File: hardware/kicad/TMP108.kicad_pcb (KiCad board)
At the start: 2 copper layers, 75 x 75 mm, 38 parts, among them J1 Screw_Terminal_01x08, J2 Screw_Terminal_01x08, J3 CAN, SW1 PRG, SW2 BUS, SW3 PRG-VALUE, U1 Teensy_3.2, U2 TMR-1211, U3 MCP2551-I-P

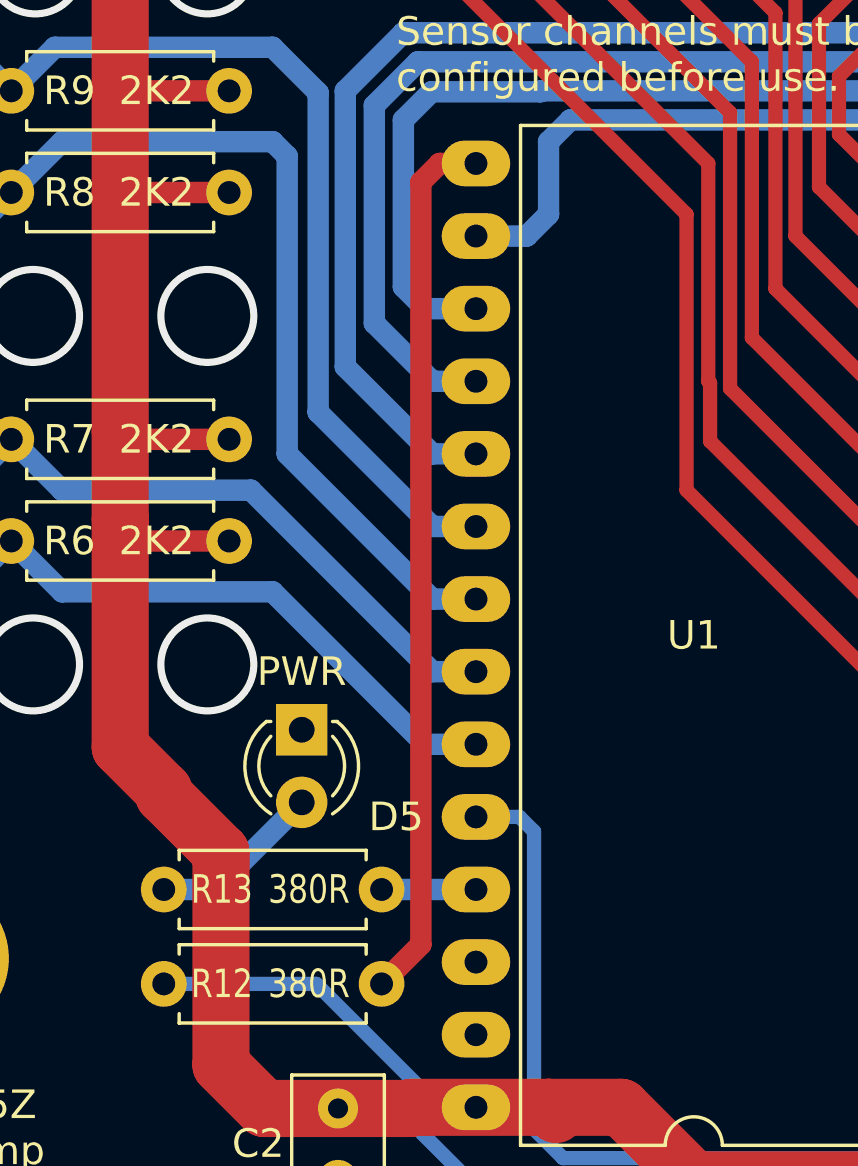
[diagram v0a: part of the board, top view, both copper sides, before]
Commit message: Reassign LED GPIO
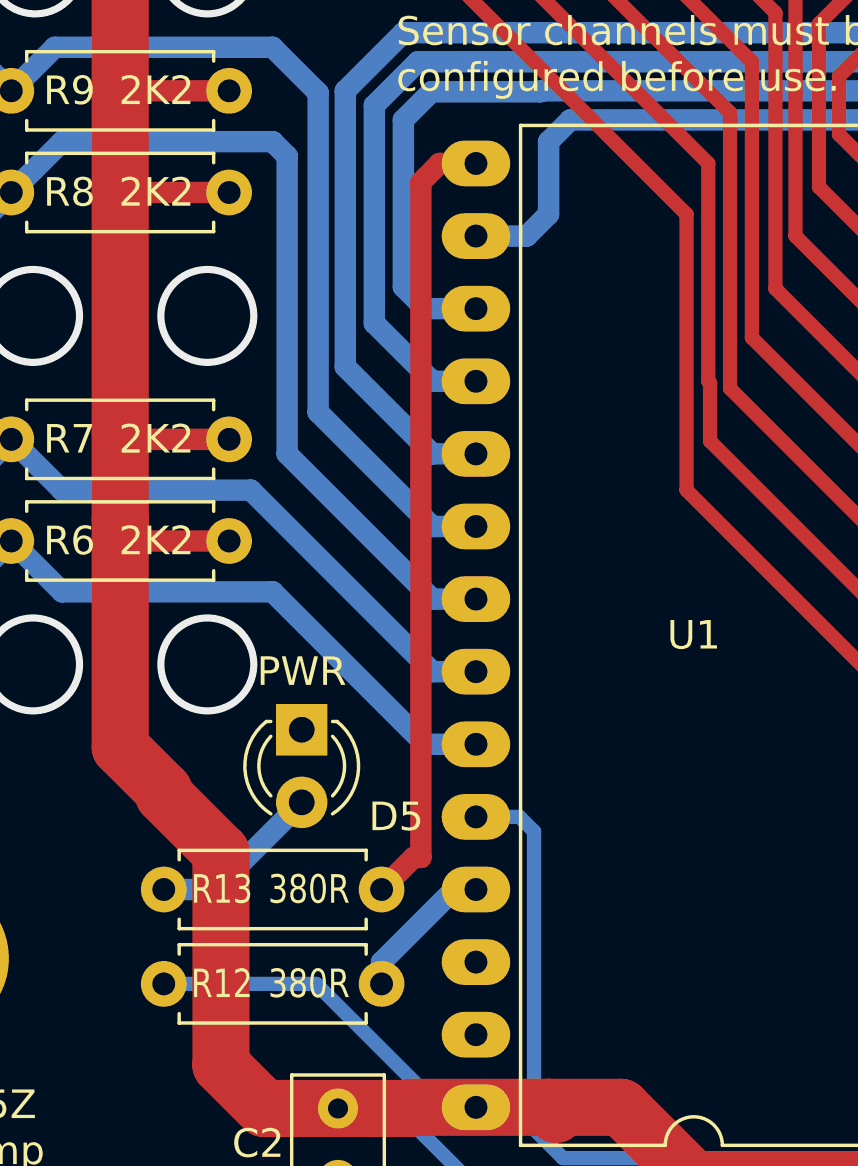
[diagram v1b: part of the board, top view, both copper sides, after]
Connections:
- U1 pad 15: /LED_INTERVAL -> /LED_PWR
- U1 pad 25: /LED_PWR -> /LED_INTERVAL
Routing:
- net /LED_INTERVAL: track 30.8 -> 5.12 mm
- net /LED_PWR: track 3.30 -> 27.7 mm

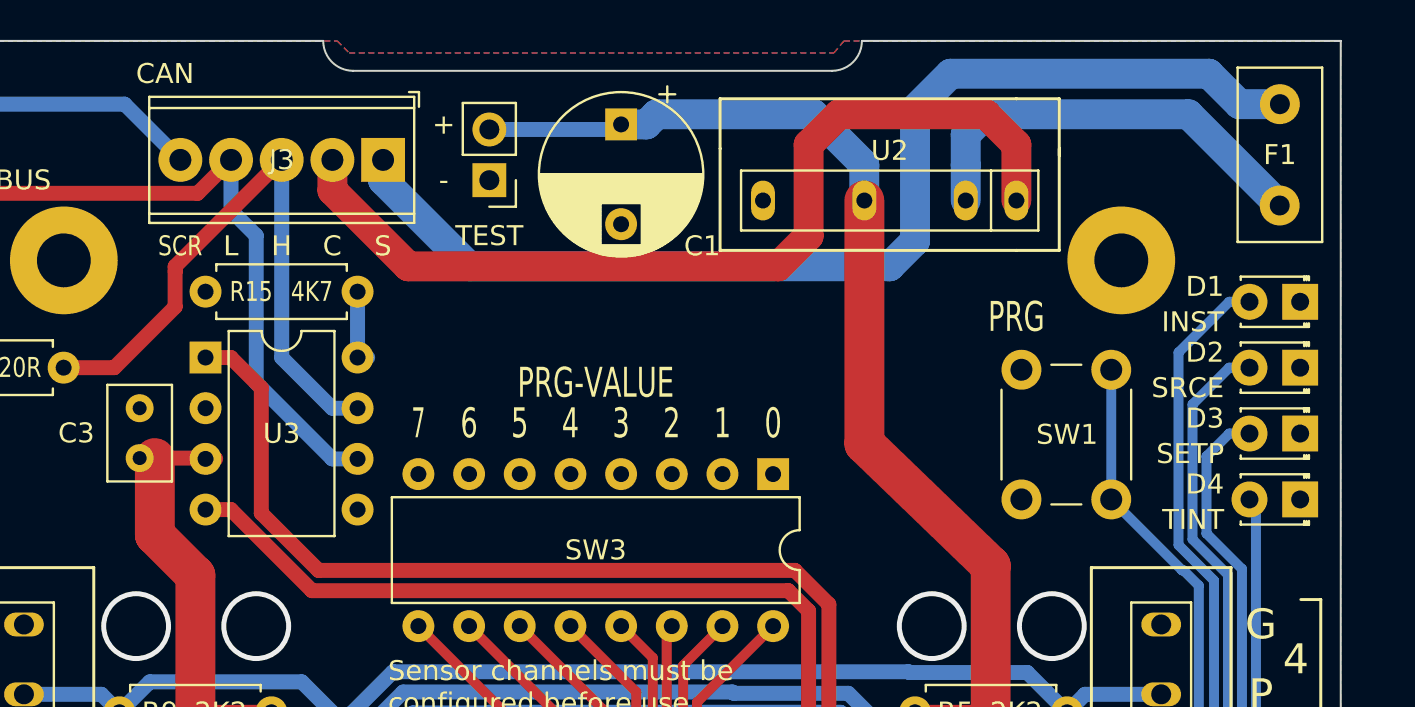
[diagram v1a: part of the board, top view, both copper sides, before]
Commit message: Reroute PCB.
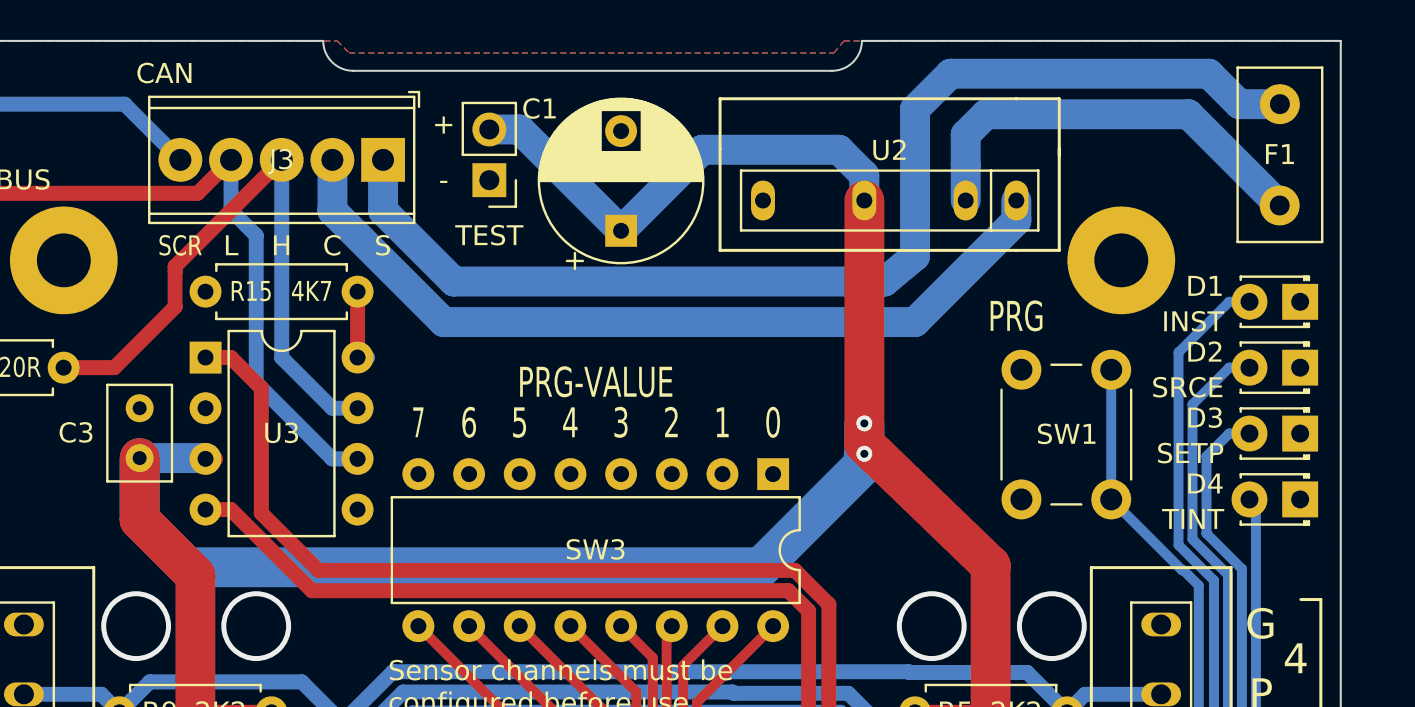
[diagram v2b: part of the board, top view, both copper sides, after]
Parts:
- moved C1 5.33 mm to (174.9, 96.5), turned to 90 degrees
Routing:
- net +5V: track 210.1 -> 257.7 mm, vias 0 -> 2
- net /NET_C: track 46.7 -> 42.3 mm
- net /NET_S: track 56.3 -> 58.2 mm

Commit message: Twaeks,
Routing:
- net /ADDR_2: track 14.6 -> 15.7 mm
- net GND: vias 12 -> 13
- net (no net): vias 0 -> 6

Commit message: Tweaks
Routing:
- net /ADDR_1: track 12.9 -> 16.4 mm
- net GND: vias 13 -> 19
- net (no net): vias 6 -> 0
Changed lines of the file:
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@@
     (thickness 1.6)
     (drawings 144)
-    (tracks 338)
+    (tracks 343)
     (zones 0)
     (modules 38)
@@
     (effects (font (size 1.5 1) (thickness 0.2)))
   )
-  (via (at 178.486 138.43) (size 0.8) (drill 0.4) (layers F.Cu B.Cu) (net 0))
-  (via (at 178.486 135.89) (size 0.8) (drill 0.4) (layers F.Cu B.Cu) (net 0))
-  (via (at 178.486 133.35) (size 0.8) (drill 0.4) (layers F.Cu B.Cu) (net 0))
-  (via (at 178.486 130.81) (size 0.8) (drill 0.4) (layers F.Cu B.Cu) (net 0))
-  (via (at 178.486 128.27) (size 0.8) (drill 0.4) (layers F.Cu B.Cu) (net 0))
-  (via (at 178.486 125.73) (size 0.8) (drill 0.4) (layers F.Cu B.Cu) (net 0))
+  (via (at 178.486 138.43) (size 0.8) (drill 0.4) (layers F.Cu B.Cu) (net 1))
+  (via (at 178.486 135.89) (size 0.8) (drill 0.4) (layers F.Cu B.Cu) (net 1))
+  (via (at 178.486 133.35) (size 0.8) (drill 0.4) (layers F.Cu B.Cu) (net 1))
+  (via (at 178.486 130.81) (size 0.8) (drill 0.4) (layers F.Cu B.Cu) (net 1))
+  (via (at 178.486 128.27) (size 0.8) (drill 0.4) (layers F.Cu B.Cu) (net 1))
+  (via (at 178.486 125.73) (size 0.8) (drill 0.4) (layers F.Cu B.Cu) (net 1))
   (via (at 178.486 123.19) (size 0.8) (drill 0.4) (layers F.Cu B.Cu) (net 1))
   (via (at 156.642 128.524) (size 3.5) (drill 3) (layers F.Cu B.Cu) (net 1))
@@
   (segment (start 177.47 117.348) (end 175.946 118.872) (width 0.5) (layer F.Cu) (net 24))
   (segment (start 177.47 116.332) (end 177.47 117.348) (width 0.5) (layer F.Cu) (net 24))
-  (segment (start 177.47 123.444) (end 179.756 125.73) (width 0.25) (layer F.Cu) (net 25))
-  (segment (start 177.47 119.888) (end 177.47 123.444) (width 0.25) (layer F.Cu) (net 25))
-  (segment (start 180.01 117.348) (end 177.47 119.888) (width 0.25) (layer F.Cu) (net 25))
-  (segment (start 180.01 116.332) (end 180.01 117.348) (width 0.25) (layer F.Cu) (net 25))
-  (segment (start 179.756 125.73) (end 181.28 125.73) (width 0.25) (layer F.Cu) (net 25))
-  (segment (start 182.55 116.332) (end 182.55 117.348) (width 0.25) (layer F.Cu) (net 26))
-  (segment (start 182.55 117.348) (end 178.994 120.904) (width 0.25) (layer F.Cu) (net 26))
-  (segment (start 178.994 120.904) (end 178.994 122.428) (width 0.25) (layer F.Cu) (net 26))
-  (segment (start 178.994 122.428) (end 179.756 123.19) (width 0.25) (layer F.Cu) (net 26))
-  (segment (start 179.756 123.19) (end 181.28 123.19) (width 0.25) (layer F.Cu) (net 26))
+  (segment (start 179.756 125.73) (end 179.629 125.603) (width 0.5) (layer F.Cu) (net 25))
+  (segment (start 181.28 125.73) (end 179.756 125.73) (width 0.5) (layer F.Cu) (net 25))
+  (segment (start 177.47 123.444) (end 179.629 125.603) (width 0.25) (layer F.Cu) (net 25))
+  (segment (start 179.756 125.718002) (end 177.47 123.432002) (width 0.5) (layer F.Cu) (net 25))
+  (segment (start 179.756 125.73) (end 179.756 125.718002) (width 0.5) (layer F.Cu) (net 25))
+  (segment (start 177.47 123.432002) (end 177.47 123.19) (width 0.5) (layer F.Cu) (net 25))
+  (segment (start 177.47 123.19) (end 177.47 123.444) (width 0.25) (layer F.Cu) (net 25))
+  (segment (start 177.47 123.19) (end 177.47 119.888) (width 0.5) (layer F.Cu) (net 25))
+  (segment (start 177.47 119.888) (end 180.01 117.348) (width 0.5) (layer F.Cu) (net 25))
+  (segment (start 180.01 117.348) (end 180.01 116.332) (width 0.5) (layer F.Cu) (net 25))
+  (segment (start 181.28 123.19) (end 179.756 123.19) (width 0.5) (layer F.Cu) (net 26))
+  (segment (start 179.756 123.19) (end 178.994 122.428) (width 0.5) (layer F.Cu) (net 26))
+  (segment (start 178.994 122.428) (end 178.994 120.904) (width 0.5) (layer F.Cu) (net 26))
+  (segment (start 178.994 120.904) (end 182.55 117.348) (width 0.5) (layer F.Cu) (net 26))
+  (segment (start 182.55 117.348) (end 182.55 116.332) (width 0.5) (layer F.Cu) (net 26))
   (segment (start 202.87 112.268) (end 202.87 102.616) (width 0.5) (layer B.Cu) (net 27))
   (segment (start 204.648 114.046) (end 202.87 112.268) (width 0.5) (layer B.Cu) (net 27))
@@
     (connect_pads (clearance 0.508))
     (min_thickness 0.254)
-    (fill (arc_segments 32) (thermal_gap 0.508) (thermal_bridge_width 0.508))
+    (fill yes (arc_segments 32) (thermal_gap 0.508) (thermal_bridge_width 0.508))
     (polygon
       (pts
@@
     (connect_pads (clearance 0.508))
     (min_thickness 0.254)
-    (fill (arc_segments 32) (thermal_gap 0.508) (thermal_bridge_width 0.508))
+    (fill yes (arc_segments 32) (thermal_gap 0.508) (thermal_bridge_width 0.508))
     (polygon
       (pts

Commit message: Isolate temperature sensors
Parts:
- removed D3: SETP, LED_THT:LED_D1.8mm_W3.3mm_H2.4mm
- removed D4: TINT, LED_THT:LED_D1.8mm_W3.3mm_H2.4mm
- removed D5: PWR, LED_THT:LED_D3.0mm_FlatTop
- removed F1: 1A, Fuse:Fuse_Littelfuse_395Series
- removed R10, R11, R12, R13: 380R, Resistor_THT:R_Axial_DIN0207_L6.3mm_D2.5mm_P7.62mm_Horizontal
- removed R14: 120R, Resistor_THT:R_Axial_DIN0207_L6.3mm_D2.5mm_P7.62mm_Horizontal
- removed R15: 4K7, Resistor_THT:R_Axial_DIN0207_L6.3mm_D2.5mm_P7.62mm_Horizontal
- removed R3, R4, R5, R6, R7, R8, R9: 2K2, Resistor_THT:R_Axial_DIN0207_L6.3mm_D2.5mm_P7.62mm_Horizontal
- removed the REF** at (200.0, 151.0)
- removed the REF** at (147.0, 151.0)
- removed the REF** at (147.0, 98.0)
- removed the REF** at (200.0, 98.0)
- removed SW1: PRG, Button_Switch_THT:SW_PUSH_6mm_H4.3mm
- removed SW2: BUS, Package_DIP:DIP-4_W7.62mm_LongPads
- removed SW3: PRG-VALUE, Package_DIP:DIP-16_W7.62mm
- removed TEST: PinHeader_1x02_P2.54mm_Vertical, Connector_PinHeader_2.54mm:PinHeader_1x02_P2.54mm_Vertical
- added C101: 100nF, Capacitor_THT:CP_Radial_D5.0mm_P2.50mm, F.Cu at (108.7, -158.1)
- added C102: 100nF, Capacitor_SMD:C_0805_2012Metric, F.Cu at (92.5, -142.5)
- added C103: 100nF, Capacitor_SMD:C_0805_2012Metric, F.Cu at (121.3, -124.1)
- added C104: 100nF, Capacitor_SMD:C_0805_2012Metric, F.Cu at (146.8, -137.5)
- added C105: 100nF, Capacitor_SMD:C_0805_2012Metric, F.Cu at (146.8, -125.5)
- added C4: 20nF, Capacitor_SMD:C_0805_2012Metric, F.Cu at (90.6, -86.1)
- added D101: LED, LED_THT:LED_D1.8mm_W3.3mm_H2.4mm, F.Cu at (166.2, -146.7)
- added D102: LED, LED_THT:LED_D1.8mm_W3.3mm_H2.4mm, F.Cu at (166.2, -143.4)
- added D103: LED, LED_THT:LED_D1.8mm_W3.3mm_H2.4mm, F.Cu at (166.2, -136.8)
- added D104: LED, LED_THT:LED_D1.8mm_W3.3mm_H2.4mm, F.Cu at (166.2, -130.2)
- added D105: LED, LED_THT:LED_D1.8mm_W3.3mm_H2.4mm, F.Cu at (166.2, -123.6)
- added D110: LED, LED_THT:LED_D1.8mm_W3.3mm_H2.4mm, F.Cu at (166.2, -140.1)
- added D111: LED, LED_THT:LED_D1.8mm_W3.3mm_H2.4mm, F.Cu at (166.2, -133.5)
- added D112: LED, LED_THT:LED_D1.8mm_W3.3mm_H2.4mm, F.Cu at (166.2, -126.9)
- added D113: LED, LED_THT:LED_D1.8mm_W3.3mm_H2.4mm, F.Cu at (166.2, -120.3)
- added F101: 1A, Fuse:Fuse_Littelfuse_395Series, F.Cu at (81.2, -152.2)
- added J101: CAN, Connector_PinHeader_2.54mm:PinHeader_1x05_P2.54mm_Vertical, F.Cu at (75.7, -147.5)
- added J4: Screw_Terminal_01x03, Connector_PinHeader_2.54mm:PinHeader_1x03_P2.54mm_Vertical, F.Cu at (124.1, -80.6)
- added J5: Screw_Terminal_01x03, Connector_PinHeader_2.54mm:PinHeader_1x03_P2.54mm_Vertical, F.Cu at (134.3, -80.6)
- added J6: Screw_Terminal_01x03, Connector_PinHeader_2.54mm:PinHeader_1x03_P2.54mm_Vertical, F.Cu at (144.5, -80.6)
- added Q101: BSS138, Package_TO_SOT_SMD:SOT-23, F.Cu at (100.4, -141.8)
- added Q102: BSS138, Package_TO_SOT_SMD:SOT-23, F.Cu at (100.4, -134.6)
- added R101: 10K 0.125W, Resistor_SMD:R_0805_2012Metric, F.Cu at (103.4, -134.6)
- added R102: 10K 0.125W, Resistor_SMD:R_0805_2012Metric, F.Cu at (103.4, -141.8)
- added R103: 10K 0.125W, Resistor_SMD:R_0805_2012Metric, F.Cu at (96.8, -142.6)
- added R104: 10K 0.125W, Resistor_SMD:R_0805_2012Metric, F.Cu at (96.8, -133.8)
- added R105: 560R, Resistor_SMD:R_0805_2012Metric, F.Cu at (169.2, -146.7)
- added R106: 4K7 0.125W, Resistor_SMD:R_0805_2012Metric, F.Cu at (84.1, -138.4)
- added R107: 120R 0.5W, Resistor_THT:R_Axial_DIN0207_L6.3mm_D2.5mm_P7.62mm_Horizontal, F.Cu at (84.8, -147.5)
- added R108: 4K7 0.125W, Resistor_SMD:R_0805_2012Metric, B.Cu at (162.9, -154.7)
- added R109: 4K7 0.125W, Resistor_SMD:R_0805_2012Metric, B.Cu at (160.4, -154.7)
- added R110: 4K7 0.125W, Resistor_SMD:R_0805_2012Metric, B.Cu at (157.9, -154.7)
- added R111: 4K7 0.125W, Resistor_SMD:R_0805_2012Metric, B.Cu at (155.3, -154.7)
- added R112: 4K7 0.125W, Resistor_SMD:R_0805_2012Metric, B.Cu at (152.8, -154.7)
- added R113: 4K7 0.125W, Resistor_SMD:R_0805_2012Metric, B.Cu at (150.2, -154.7)
- added R114: 4K7 0.125W, Resistor_SMD:R_0805_2012Metric, B.Cu at (147.7, -154.7)
- added R115: 4K7 0.125W, Resistor_SMD:R_0805_2012Metric, B.Cu at (145.2, -154.7)
- added R116: 560R, Resistor_SMD:R_0805_2012Metric, F.Cu at (169.2, -143.4)
- added R117: 560R, Resistor_SMD:R_0805_2012Metric, F.Cu at (169.2, -140.1)
- added R118: 560R, Resistor_SMD:R_0805_2012Metric, F.Cu at (169.2, -136.8)
- added R119: 560R, Resistor_SMD:R_0805_2012Metric, F.Cu at (169.2, -133.5)
- added R120: 560R, Resistor_SMD:R_0805_2012Metric, F.Cu at (169.2, -130.2)
- added R121: 560R, Resistor_SMD:R_0805_2012Metric, F.Cu at (169.2, -127.0)
- added R122: 560R, Resistor_SMD:R_0805_2012Metric, F.Cu at (169.2, -123.6)
- added R123: 560R, Resistor_SMD:R_0805_2012Metric, F.Cu at (169.2, -120.3)
- added REF**: MountingHole_3.2mm_M3_DIN965_Pad_TopBottom, MountingHole:MountingHole_3.2mm_M3_DIN965_Pad_TopBottom, F.Cu at (167.6, -82.4)
- added REF**: MountingHole_3.2mm_M3_DIN965_Pad_TopBottom, MountingHole:MountingHole_3.2mm_M3_DIN965_Pad_TopBottom, F.Cu at (75.6, -153.4)
- added REF**: MountingHole_3.2mm_M3_DIN965_Pad_TopBottom, MountingHole:MountingHole_3.2mm_M3_DIN965_Pad_TopBottom, F.Cu at (167.6, -153.4)
- added REF**: MountingHole_3.2mm_M3_DIN965_Pad_TopBottom, MountingHole:MountingHole_3.2mm_M3_DIN965_Pad_TopBottom, F.Cu at (75.6, -82.4)
- added REF**: TestPoint_THTPad_1.5x1.5mm_Drill0.7mm, TestPoint:TestPoint_THTPad_1.5x1.5mm_Drill0.7mm, F.Cu at (74.8, -133.3)
- added SW101: BUS, Package_DIP:DIP-4_W7.62mm_LongPads, F.Cu at (96.5, -147.9)
- added SW102: ADDR/VALUE, Package_DIP:DIP-16_W7.62mm, F.Cu at (145.2, -150.9)
- added SW103: PRG, Button_Switch_THT:SW_TH_Tactile_Omron_B3F-10xx, F.Cu at (112.8, -156.0)
- added TEST 5V0: TestPoint_THTPad_1.5x1.5mm_Drill0.7mm, TestPoint:TestPoint_THTPad_1.5x1.5mm_Drill0.7mm, F.Cu at (81.2, -133.3)
- added TEST 5V0: TestPoint_THTPad_1.5x1.5mm_Drill0.7mm, TestPoint:TestPoint_THTPad_1.5x1.5mm_Drill0.7mm, F.Cu at (78.0, -133.3)
- added U101: TMR-2-2411, PDJR_DC-DC_Converters:TMR_2411, F.Cu at (85.9, -156.0)
- added U102: MCP2551-I-P, Package_SO:SOIC-8_3.9x4.9mm_P1.27mm, F.Cu at (87.5, -142.5)
- added U103: Teensy_4.0, Package_DIP:DIP-28_W15.24mm_LongPads, F.Cu at (139.3, -123.0)
- added U104: 74HC165, Package_SO:SO-16_3.9x9.9mm_P1.27mm, F.Cu at (151.8, -142.9)
- added U105: 74HCT595, Package_SO:SO-16_3.9x9.9mm_P1.27mm, F.Cu at (151.8, -130.9)
- C1: value 1000uF -> 10uF; footprint Capacitor_THT:CP_Radial_D8.0mm_P5.00mm -> Capacitor_SMD:C_0805_2012Metric
- C2: value 100nF -> 20nF; footprint Capacitor_THT:C_Rect_L4.6mm_W3.0mm_P2.50mm_MKS02_FKP02 -> Capacitor_SMD:C_0805_2012Metric
- C3: value 100n -> 10uF; footprint Capacitor_THT:C_Rect_L4.6mm_W3.0mm_P2.50mm_MKS02_FKP02 -> Capacitor_SMD:C_0805_2012Metric
- D1: value INST -> MBR0520LT; footprint LED_THT:LED_D1.8mm_W3.3mm_H2.4mm -> Diode_SMD:D_SOD-123
- D2: value SRCE -> MBR0520LT; footprint LED_THT:LED_D1.8mm_W3.3mm_H2.4mm -> Diode_SMD:D_SOD-123
- J1, J2: value Screw_Terminal_01x08 -> Screw_Terminal_01x03; footprint PDJR-connectors:Phoenix-FK-MPT-8-3,5 -> Connector_PinHeader_2.54mm:PinHeader_1x03_P2.54mm_Vertical
- J3: value CAN -> Screw_Terminal_01x03; footprint TerminalBlock_Phoenix:TerminalBlock_Phoenix_MPT-0,5-5-2.54_1x05_P2.54mm_Horizontal -> Connector_PinHeader_2.54mm:PinHeader_1x03_P2.54mm_Vertical
- R1: value 380R -> 1K; footprint Resistor_THT:R_Axial_DIN0207_L6.3mm_D2.5mm_P7.62mm_Horizontal -> Resistor_SMD:R_0805_2012Metric
- R2: value 2K2 -> 1K; footprint Resistor_THT:R_Axial_DIN0207_L6.3mm_D2.5mm_P7.62mm_Horizontal -> Resistor_SMD:R_0805_2012Metric
- U1: value Teensy_3.2 -> MAX845; footprint Package_DIP:DIP-28_W15.24mm_LongPads -> Package_SO:TSSOP-8_3x3mm_P0.65mm
- U2: value TMR-1211 -> TGM-050P3RL; footprint PDJR-connectors:TMR-1-1211 -> PDJR-transformers:TGM-010P3RL
- U3: value MCP2551-I-P -> ISO1540; footprint Package_DIP:DIP-8_W7.62mm -> Package_SO:SOIC-8_3.9x4.9mm_P1.27mm
- moved U1 275.0 mm to (90.7, -103.4)
- moved C2 263.9 mm to (97.8, -100.0), turned to 180 degrees
- moved R1 259.8 mm to (101.6, -98.4), turned to 270 degrees
- moved R2 246.9 mm to (101.6, -91.2), turned to 90 degrees
- moved J1 235.5 mm to (93.7, -80.6)
- moved D2 225.5 mm to (87.7, -86.8), turned to 90 degrees
- moved D1 219.6 mm to (93.5, -86.8), turned to 90 degrees
- moved C1 214.6 mm to (95.5, -102.9), turned to 270 degrees
- moved U2 213.7 mm to (90.6, -95.0)
- moved J2 213.1 mm to (103.8, -80.6)
- moved U3 205.7 mm to (97.8, -95.0), turned to 270 degrees
- moved C3 205.0 mm to (97.7, -90.1), turned to 180 degrees
- moved J3 180.3 mm to (114.0, -80.6), turned to 90 degrees
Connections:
- C3 pad 1: +5V -> VDD
- C3 pad 2: GND -> GNDREF
- D1 pad 1: GND -> VDD
- D2 pad 1: GND -> VDD
- J1 pad 1: /SENSOR_T0 -> GNDREF
- J1 pad 2: GND -> Net-(J1-Pad2)
- J1 pad 3: /SENSOR_T1 -> VDD
- J2 pad 1: /SENSOR_T7 -> GNDREF
- J2 pad 2: GND -> Net-(J1-Pad2)
- J2 pad 3: /SENSOR_T6 -> VDD
- J3 pad 1: /NET_S -> GNDREF
- J3 pad 2: /NET_C -> Net-(J1-Pad2)
- J3 pad 3: /CAN_H -> VDD
- R1 pad 1: /LED_INSTANCE -> +5V
- R1 pad 2: Net-(D1-Pad2) -> /D23
- R2 pad 1: /SENSOR_T0 -> VDD
- R2 pad 2: +5V -> Net-(J1-Pad2)
- U1 pad 1: GND -> Net-(U1-Pad1)
- U1 pad 2: /LED_SETPOINT -> GND
- U1 pad 3: /LED_SOURCE -> +5V
- U1 pad 4: /LED_INSTANCE -> +5V
- U1 pad 5: /CAN_TX -> (no net)
- U1 pad 6: /CAN_RX -> +5V
- U1 pad 7: /ADDR_7 -> GND
- U1 pad 8: /ADDR_6 -> Net-(U1-Pad8)
- U2 pad 1: /NET_C -> Net-(U1-Pad1)
- U2 pad 2: Net-(F1-Pad2) -> +5V
- U2 pad 4: +5V -> Net-(U1-Pad8)
- U2 pad 6: GND -> GNDREF
- U3 pad 1: /CAN_TX -> +5V
- U3 pad 2: GND -> /D23
- U3 pad 3: +5V -> Net-(U3-Pad3)
- U3 pad 4: /CAN_RX -> GND
- U3 pad 5: Net-(U3-Pad5) -> GNDREF
- U3 pad 6: /CAN_L -> Net-(U3-Pad6)
- U3 pad 7: /CAN_H -> Net-(J1-Pad2)
- U3 pad 8: Net-(R15-Pad2) -> VDD
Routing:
- net +3V3: track 0.00 -> 164.9 mm, vias 0 -> 4
- net VDD: track 0.00 -> 109.4 mm
- net Net-(SW1-Pad2): track 101.1 -> 0.00 mm
- net Net-(D4-Pad2): track 98.1 -> 0.00 mm
- net Net-(J1-Pad2): track 0.00 -> 82.0 mm
- net /D23: track 0.00 -> 63.7 mm, vias 0 -> 1
- net Net-(D3-Pad2): track 59.6 -> 0.00 mm
- net /NET_S: track 58.2 -> 0.00 mm
- net /SENSOR_T3: track 58.1 -> 0.00 mm
- net Net-(D2-Pad2): track 59.7 -> 2.69 mm
- net Net-(D1-Pad2): track 59.7 -> 2.69 mm
- net /SENSOR_T1: track 55.1 -> 0.00 mm
- net /SENSOR_T2: track 55.1 -> 0.00 mm
- net Net-(D101-Pad2): track 0.00 -> 51.0 mm, vias 0 -> 1
- net /SENSOR_T0: track 50.2 -> 0.00 mm
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- added copper zone on B.Cu, net GNDREF
- added copper zone on F.Cu, net GNDREF
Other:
- board size 75 x 75 mm -> 100 x 85 mm
- board text added: "128"
- board text added: "16"
- board text added: "32"
- board text added: "3V3"
- board text added: "5V0"
- board text added: "64"
- board text added: "CONNECT BUS SHIELD TO GROUND"
- board text added: "D23 - D16"
- board text added: "D9 - D5"
- board text added: "GND"
- board text added: "TERMINATE BUS"
- board text removed: "+"
- board text removed: "-"
- board text removed: "0"
- board text removed: "2022 (c) PDJR"
- board text removed: "3"
- board text removed: "5"
- board text removed: "6"
- board text removed: "7"
- board text removed: "G"
- board text removed: "NMEA 2000 Temperature Sensor Module"
- board text removed: "P"
- board text removed: "PWR/TX"
- board text removed: "Sensor channels must be configured before use."
- board text removed: "T"
- board text removed: "TMP108.2"
- board text removed: "TSENSE"
- board text removed: "USE ONLY LM335Z or equivalent temp sensors."
